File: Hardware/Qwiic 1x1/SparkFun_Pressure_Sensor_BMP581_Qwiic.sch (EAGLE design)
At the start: 25 parts, among them J1 QWIIC_RIGHT_ANGLE, J2 QWIIC_RIGHT_ANGLE, U1 BMP581

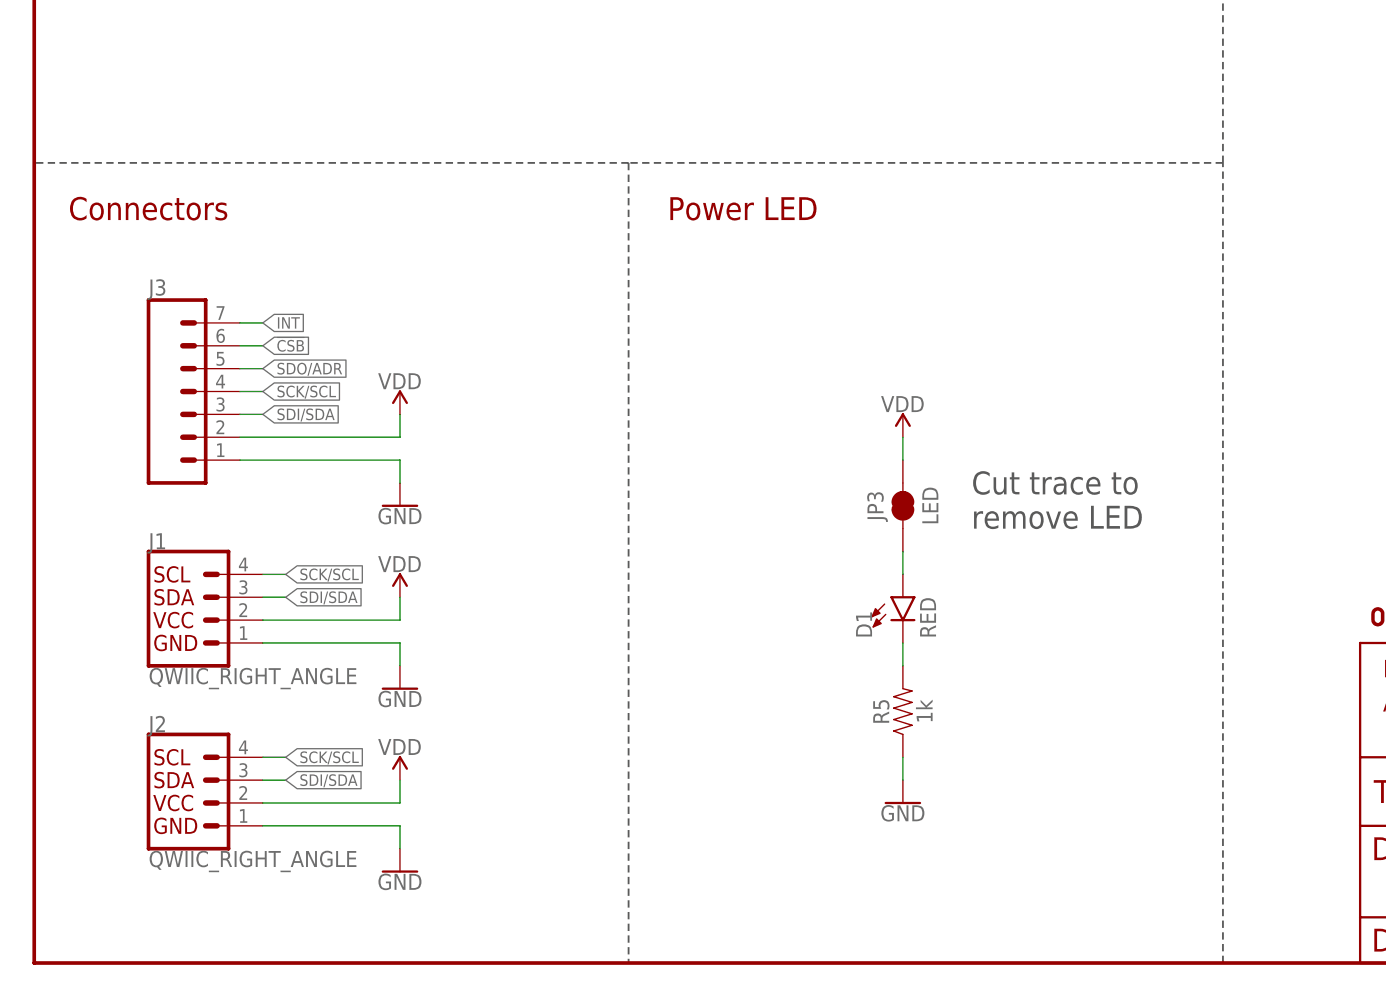
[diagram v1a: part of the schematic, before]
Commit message: Add optional pullup on CSB
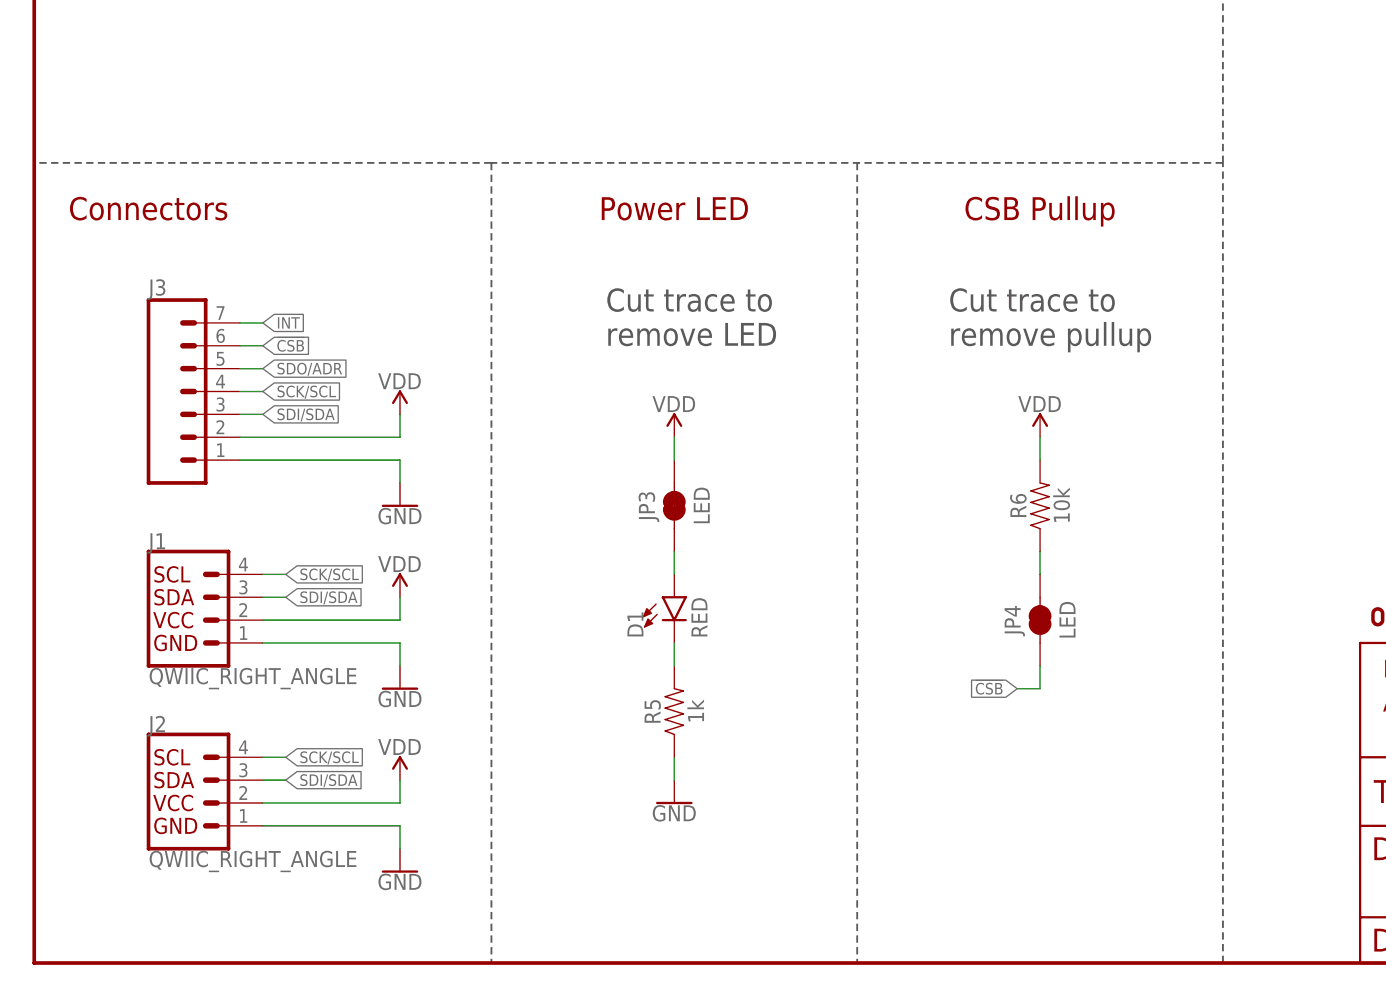
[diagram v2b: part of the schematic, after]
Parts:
- added JP4: LED, SparkFun-Jumpers:JUMPER-SMT_2_NC_TRACE_SILK
- added R6: 10k, SparkFun-Resistors:10KOHM-0603-1/10W-1%
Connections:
- new net N$7: JP4.2, R6.1
- net !CSB!: now also JP4.1
- net VDD: now also R6.2
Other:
- note added: "CSB Pullup"
- note added: "Cut trace to remove pullup"
- moved on the sheet: D1, JP3, R5
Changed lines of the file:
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@@
 <part name="LOGO4" library="SparkFun-Aesthetics" deviceset="SFE_LOGO_NAME_FLAME" device=".1_INCH"/>
 <part name="U1" library="BMP581" deviceset="BMP581" device=""/>
+<part name="JP4" library="SparkFun-Jumpers" deviceset="JUMPER-SMT_2_NC_TRACE" device="_SILK" package3d_urn="urn:adsk.eagle:package:39281/1" value="LED"/>
+<part name="SUPPLY8" library="SparkFun-PowerSymbols" deviceset="VDD" device=""/>
+<part name="R6" library="SparkFun-Resistors" deviceset="10KOHM" device="-0603-1/10W-1%" value="10k"/>
 </parts>
 <sheets>
@@
 <wire x1="132.08" y1="88.9" x2="132.08" y2="114.3" width="0.2032" layer="97" style="shortdash"/>
 <wire x1="132.08" y1="114.3" x2="132.08" y2="185.42" width="0.2032" layer="97" style="shortdash"/>
-<wire x1="132.08" y1="88.9" x2="66.04" y2="88.9" width="0.2032" layer="97" style="shortdash"/>
+<wire x1="132.08" y1="88.9" x2="50.8" y2="88.9" width="0.2032" layer="97" style="shortdash"/>
 <text x="12.7" y="83.82" size="2.54" layer="94" font="vector" align="center">Connectors</text>
 <text x="25.4" y="180.34" size="2.54" layer="94" font="vector" align="center">Pressure Sensor - BMP581</text>
@@
 <text x="220.98" y="88.9" size="2.54" layer="97" font="vector">0x46</text>
 <text x="220.98" y="81.28" size="2.54" layer="97" font="vector">0x47</text>
-<wire x1="66.04" y1="88.9" x2="0" y2="88.9" width="0.2032" layer="97" style="shortdash"/>
+<wire x1="50.8" y1="88.9" x2="0" y2="88.9" width="0.2032" layer="97" style="shortdash"/>
 <wire x1="193.04" y1="101.6" x2="193.04" y2="93.98" width="0.2032" layer="97"/>
 <wire x1="193.04" y1="93.98" x2="193.04" y2="86.36" width="0.2032" layer="97"/>
@@
 <wire x1="53.34" y1="167.64" x2="27.94" y2="167.64" width="0.2032" layer="97"/>
 <wire x1="27.94" y1="160.02" x2="53.34" y2="160.02" width="0.2032" layer="97"/>
-<wire x1="66.04" y1="88.9" x2="66.04" y2="0" width="0.2032" layer="97" style="shortdash"/>
-<text x="78.74" y="83.82" size="2.54" layer="94" font="vector" align="center">Power LED</text>
+<wire x1="50.8" y1="88.9" x2="50.8" y2="0" width="0.2032" layer="97" style="shortdash"/>
+<text x="71.12" y="83.82" size="2.54" layer="94" font="vector" align="center">Power LED</text>
 <text x="88.9" y="162.56" size="2.54" layer="97" font="vector">WARNING</text>
 <text x="81.28" y="147.32" size="2.54" layer="97" font="vector">Interface pins should
@@
 <wire x1="78.74" y1="160.02" x2="78.74" y2="144.78" width="0.2032" layer="97"/>
 <wire x1="78.74" y1="144.78" x2="116.84" y2="144.78" width="0.2032" layer="97"/>
-<text x="104.14" y="48.26" size="2.54" layer="97" font="vector">Cut trace to
+<text x="63.5" y="68.58" size="2.54" layer="97" font="vector">Cut trace to
 remove LED</text>
+<wire x1="91.44" y1="88.9" x2="91.44" y2="0" width="0.2032" layer="97" style="shortdash"/>
+<text x="111.76" y="83.82" size="2.54" layer="94" font="vector" align="center">CSB Pullup</text>
+<text x="101.6" y="68.58" size="2.54" layer="97" font="vector">Cut trace to
+remove pullup</text>
 </plain>
 <instances>
@@
 <attribute name="VALUE" x="187.198" y="140.716" size="1.778" layer="96" font="vector" align="center"/>
 </instance>
-<instance part="D1" gate="G$1" x="96.52" y="40.64" smashed="yes">
-<attribute name="NAME" x="93.091" y="36.068" size="1.778" layer="95" font="vector" rot="R90"/>
-<attribute name="VALUE" x="98.425" y="36.068" size="1.778" layer="96" font="vector" rot="R90" align="top-left"/>
-</instance>
-<instance part="R5" gate="G$1" x="96.52" y="27.94" smashed="yes" rot="R90">
-<attribute name="NAME" x="94.996" y="27.94" size="1.778" layer="95" font="vector" rot="R90" align="bottom-center"/>
-<attribute name="VALUE" x="98.044" y="27.94" size="1.778" layer="96" font="vector" rot="R90" align="top-center"/>
-</instance>
-<instance part="JP3" gate="G$1" x="96.52" y="50.8" smashed="yes" rot="R90">
-<attribute name="NAME" x="93.472" y="50.8" size="1.778" layer="95" font="vector" rot="R90" align="center"/>
-<attribute name="VALUE" x="99.568" y="50.8" size="1.778" layer="96" font="vector" rot="R90" align="center"/>
-</instance>
-<instance part="SUPPLY4" gate="VDD" x="96.52" y="58.42" smashed="yes">
-<attribute name="VALUE" x="96.52" y="61.214" size="1.778" layer="96" align="bottom-center"/>
-</instance>
-<instance part="GND7" gate="1" x="96.52" y="17.78" smashed="yes">
-<attribute name="VALUE" x="96.52" y="17.526" size="1.778" layer="96" align="top-center"/>
+<instance part="D1" gate="G$1" x="71.12" y="40.64" smashed="yes">
+<attribute name="NAME" x="67.691" y="36.068" size="1.778" layer="95" font="vector" rot="R90"/>
+<attribute name="VALUE" x="73.025" y="36.068" size="1.778" layer="96" font="vector" rot="R90" align="top-left"/>
+</instance>
+<instance part="R5" gate="G$1" x="71.12" y="27.94" smashed="yes" rot="R90">
+<attribute name="NAME" x="69.596" y="27.94" size="1.778" layer="95" font="vector" rot="R90" align="bottom-center"/>
+<attribute name="VALUE" x="72.644" y="27.94" size="1.778" layer="96" font="vector" rot="R90" align="top-center"/>
+</instance>
+<instance part="JP3" gate="G$1" x="71.12" y="50.8" smashed="yes" rot="R90">
+<attribute name="NAME" x="68.072" y="50.8" size="1.778" layer="95" font="vector" rot="R90" align="center"/>
+<attribute name="VALUE" x="74.168" y="50.8" size="1.778" layer="96" font="vector" rot="R90" align="center"/>
+</instance>
+<instance part="SUPPLY4" gate="VDD" x="71.12" y="58.42" smashed="yes">
+<attribute name="VALUE" x="71.12" y="61.214" size="1.778" layer="96" align="bottom-center"/>
+</instance>
+<instance part="GND7" gate="1" x="71.12" y="17.78" smashed="yes">
+<attribute name="VALUE" x="71.12" y="17.526" size="1.778" layer="96" align="top-center"/>
 </instance>
 <instance part="LOGO2" gate="G$1" x="223.012" y="45.466" smashed="yes"/>
@@
 <attribute name="NAME" x="55.88" y="134.874" size="1.778" layer="95" font="vector"/>
 <attribute name="VALUE" x="55.88" y="114.3" size="1.778" layer="96" font="vector"/>
+</instance>
+<instance part="JP4" gate="G$1" x="111.76" y="38.1" smashed="yes" rot="R90">
+<attribute name="NAME" x="108.712" y="38.1" size="1.778" layer="95" font="vector" rot="R90" align="center"/>
+<attribute name="VALUE" x="114.808" y="38.1" size="1.778" layer="96" font="vector" rot="R90" align="center"/>
+</instance>
+<instance part="SUPPLY8" gate="VDD" x="111.76" y="58.42" smashed="yes">
+<attribute name="VALUE" x="111.76" y="61.214" size="1.778" layer="96" align="bottom-center"/>
+</instance>
+<instance part="R6" gate="G$1" x="111.76" y="50.8" smashed="yes" rot="R90">
+<attribute name="NAME" x="110.236" y="50.8" size="1.778" layer="95" font="vector" rot="R90" align="bottom-center"/>
+<attribute name="VALUE" x="113.284" y="50.8" size="1.778" layer="96" font="vector" rot="R90" align="top-center"/>
 </instance>
 </instances>
@@
 <pinref part="JP3" gate="G$1" pin="2"/>
 <pinref part="SUPPLY4" gate="VDD" pin="VDD"/>
-<wire x1="96.52" y1="55.88" x2="96.52" y2="58.42" width="0.1524" layer="91"/>
+<wire x1="71.12" y1="55.88" x2="71.12" y2="58.42" width="0.1524" layer="91"/>
+</segment>
+<segment>
+<pinref part="R6" gate="G$1" pin="2"/>
+<pinref part="SUPPLY8" gate="VDD" pin="VDD"/>
+<wire x1="111.76" y1="55.88" x2="111.76" y2="58.42" width="0.1524" layer="91"/>
 </segment>
 </net>
@@
 <pinref part="GND7" gate="1" pin="GND"/>
 <pinref part="R5" gate="G$1" pin="1"/>
-<wire x1="96.52" y1="20.32" x2="96.52" y2="22.86" width="0.1524" layer="91"/>
+<wire x1="71.12" y1="20.32" x2="71.12" y2="22.86" width="0.1524" layer="91"/>
 </segment>
 </net>
@@
 <label x="25.4" y="68.58" size="1.27" layer="95" xref="yes"/>
 </segment>
+<segment>
+<wire x1="111.76" y1="30.48" x2="109.22" y2="30.48" width="0.1524" layer="91"/>
+<label x="109.22" y="30.48" size="1.27" layer="95" font="vector" rot="R180" xref="yes"/>
+<pinref part="JP4" gate="G$1" pin="1"/>
+<wire x1="111.76" y1="30.48" x2="111.76" y2="33.02" width="0.1524" layer="91"/>
+</segment>
 </net>
 <net name="N$1" class="0">
@@
 <pinref part="JP3" gate="G$1" pin="1"/>
 <pinref part="D1" gate="G$1" pin="A"/>
-<wire x1="96.52" y1="45.72" x2="96.52" y2="43.18" width="0.1524" layer="91"/>
+<wire x1="71.12" y1="45.72" x2="71.12" y2="43.18" width="0.1524" layer="91"/>
 </segment>
 </net>
@@
 <pinref part="D1" gate="G$1" pin="C"/>
 <pinref part="R5" gate="G$1" pin="2"/>
-<wire x1="96.52" y1="35.56" x2="96.52" y2="33.02" width="0.1524" layer="91"/>
-</segment>
-</net>
+<wire x1="71.12" y1="35.56" x2="71.12" y2="33.02" width="0.1524" layer="91"/>
+</segment>
+</net>
+<net name="N$7" class="0">
+<segment>
+<pinref part="JP4" gate="G$1" pin="2"/>
+<pinref part="R6" gate="G$1" pin="1"/>
+<wire x1="111.76" y1="43.18" x2="111.76" y2="45.72" width="0.1524" layer="91"/>
+</segment>
+</net>

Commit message: Rename CSB pullup jumper in schematic
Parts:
- JP4: value LED -> !CSB!
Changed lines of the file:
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@@
 <part name="LOGO4" library="SparkFun-Aesthetics" deviceset="SFE_LOGO_NAME_FLAME" device=".1_INCH"/>
 <part name="U1" library="BMP581" deviceset="BMP581" device=""/>
-<part name="JP4" library="SparkFun-Jumpers" deviceset="JUMPER-SMT_2_NC_TRACE" device="_SILK" package3d_urn="urn:adsk.eagle:package:39281/1" value="LED"/>
+<part name="JP4" library="SparkFun-Jumpers" deviceset="JUMPER-SMT_2_NC_TRACE" device="_SILK" package3d_urn="urn:adsk.eagle:package:39281/1" value="!CSB!"/>
 <part name="SUPPLY8" library="SparkFun-PowerSymbols" deviceset="VDD" device=""/>
 <part name="R6" library="SparkFun-Resistors" deviceset="10KOHM" device="-0603-1/10W-1%" value="10k"/>

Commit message: Remove library file
BMP384 is in SFE Eagle library, update part in design
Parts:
- U1: device BMP581:BMP581 -> SparkFun-Sensors:BMP581
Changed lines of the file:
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@@
 <part name="LOGO2" library="SparkFun-Aesthetics" deviceset="SFE_LOGO_FLAME" device=".2_INCH"/>
 <part name="LOGO4" library="SparkFun-Aesthetics" deviceset="SFE_LOGO_NAME_FLAME" device=".1_INCH"/>
-<part name="U1" library="BMP581" deviceset="BMP581" device=""/>
+<part name="U1" library="SparkFun-Sensors" deviceset="BMP581" device=""/>
 <part name="JP4" library="SparkFun-Jumpers" deviceset="JUMPER-SMT_2_NC_TRACE" device="_SILK" package3d_urn="urn:adsk.eagle:package:39281/1" value="!CSB!"/>
 <part name="SUPPLY8" library="SparkFun-PowerSymbols" deviceset="VDD" device=""/>
